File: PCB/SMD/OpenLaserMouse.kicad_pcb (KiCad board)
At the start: 2 copper layers, 56 x 84 mm, 24 parts, among them J1 Amiga_Conn, M1 ADNS-9800, Q1 IRLML6302TRPBF, SW2 LEFT, SW3 RIGHT

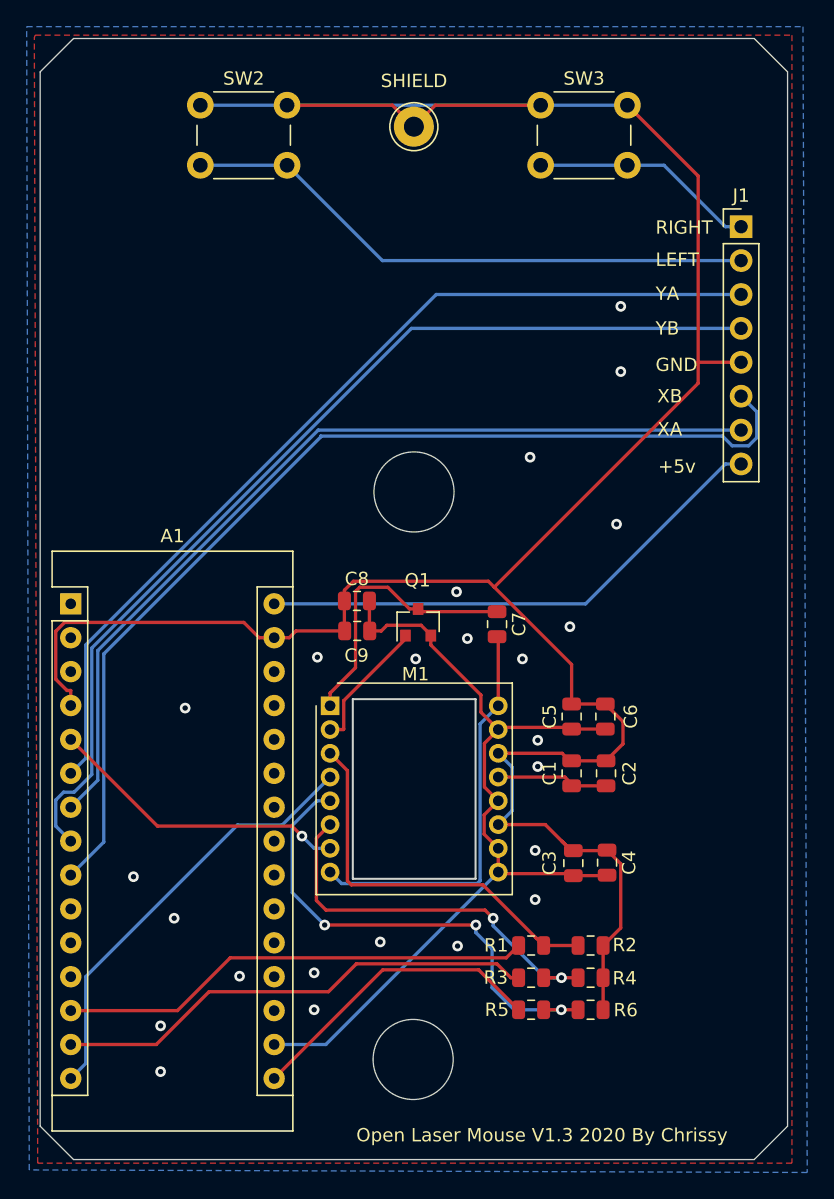
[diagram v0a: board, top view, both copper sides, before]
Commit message: Added ST Mouse PCB
Added ST Mouse PCB
Fixed Wrong Fillplane on Amiga PCB
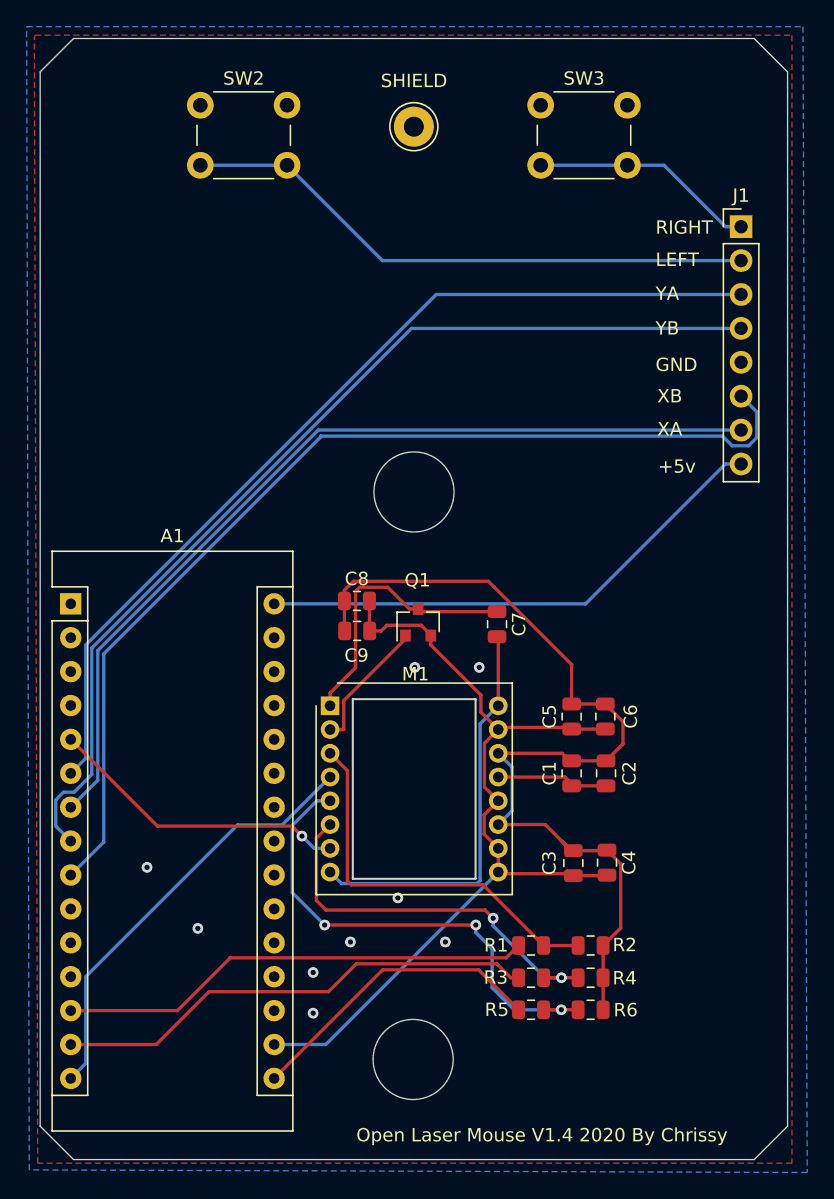
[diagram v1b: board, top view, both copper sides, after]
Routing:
- net GND: track 201.2 -> 72.1 mm, vias 0 -> 9
- net Net-(A1-Pad1): vias 24 -> 0
- added copper zone on B.Cu, net GND
- added copper zone on F.Cu, net GND
- removed copper zone on B.Cu, net Net-(A1-Pad1)
- removed copper zone on F.Cu, net Net-(A1-Pad1)
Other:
- board text added: "Open Laser Mouse V1.4 2020 By Chrissy"
- board text removed: "Open Laser Mouse V1.3 2020 By Chrissy"
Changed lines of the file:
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@@
     (thickness 1.6)
     (drawings 18)
-    (tracks 242)
+    (tracks 204)
     (zones 0)
     (modules 24)
@@
     (effects (font (size 1 1) (thickness 0.15)) (justify left))
   )
-  (gr_text "Open Laser Mouse V1.3 2020 By Chrissy" (at 77.597 122.174) (layer F.SilkS)
+  (gr_text "Open Laser Mouse V1.4 2020 By Chrissy" (at 77.597 122.174) (layer F.SilkS)
     (effects (font (size 1 1) (thickness 0.15)))
   )
@@
   (segment (start 79.1055 100.1612) (end 79.9465 101.002) (width 0.25) (layer F.Cu) (net 14) (status 20))
   (segment (start 81.9145 101.002) (end 81.915 101.002) (width 0.25) (layer F.Cu) (net 14) (status 30))
-  (segment (start 42.291 89.9795) (end 42.291 88.8542) (width 0.25) (layer F.Cu) (net 14) (status 10))
-  (segment (start 57.531 84.8995) (end 56.4057 84.8995) (width 0.25) (layer F.Cu) (net 14) (status 10))
-  (segment (start 56.4057 84.8995) (end 55.2596 83.7534) (width 0.25) (layer F.Cu) (net 14))
-  (segment (start 55.2596 83.7534) (end 41.8286 83.7534) (width 0.25) (layer F.Cu) (net 14))
-  (segment (start 41.8286 83.7534) (end 41.1657 84.4163) (width 0.25) (layer F.Cu) (net 14))
-  (segment (start 41.1657 84.4163) (end 41.1657 88.0103) (width 0.25) (layer F.Cu) (net 14))
-  (segment (start 41.1657 88.0103) (end 42.0096 88.8542) (width 0.25) (layer F.Cu) (net 14))
-  (segment (start 42.0096 88.8542) (end 42.291 88.8542) (width 0.25) (layer F.Cu) (net 14))
-  (segment (start 57.531 84.8995) (end 58.6563 84.8995) (width 0.25) (layer F.Cu) (net 14) (status 10))
-  (segment (start 58.6563 84.8995) (end 59.1643 84.3915) (width 0.25) (layer F.Cu) (net 14))
-  (segment (start 59.1643 84.3915) (end 62.9665 84.3915) (width 0.25) (layer F.Cu) (net 14) (status 20))
-  (segment (start 89.3011 64.262) (end 89.3011 65.8347) (width 0.25) (layer F.Cu) (net 14))
-  (segment (start 92.5195 64.262) (end 89.3011 64.262) (width 0.25) (layer F.Cu) (net 14) (status 10))
   (segment (start 62.9665 82.263) (end 62.9665 82.677) (width 0.25) (layer F.Cu) (net 14) (status 30))
   (segment (start 74.322 98.9) (end 75.3618 97.8602) (width 0.25) (layer B.Cu) (net 14) (status 10))
   (segment (start 75.3618 97.8602) (end 75.3618 94.5998) (width 0.25) (layer B.Cu) (net 14))
   (segment (start 75.3618 94.5998) (end 74.322 93.56) (width 0.25) (layer B.Cu) (net 14) (status 20))
-  (segment (start 58.5 45) (end 52 45) (width 0.25) (layer B.Cu) (net 14) (status 30))
-  (segment (start 84 45) (end 77.5 45) (width 0.25) (layer B.Cu) (net 14) (status 30))
-  (segment (start 77.5 45) (end 58.5 45) (width 0.25) (layer B.Cu) (net 14) (status 30))
   (segment (start 74.322 93.56) (end 79.1075 93.56) (width 0.25) (layer F.Cu) (net 14) (status 10))
   (segment (start 79.1075 93.56) (end 79.8195 94.272) (width 0.25) (layer F.Cu) (net 14) (status 20))
-  (segment (start 89.3011 64.262) (end 89.3011 50.3011) (width 0.25) (layer F.Cu) (net 14))
-  (segment (start 89.3011 50.3011) (end 84 45) (width 0.25) (layer F.Cu) (net 14) (status 20))
-  (segment (start 66.391 45) (end 58.5 45) (width 0.25) (layer F.Cu) (net 14) (status 20))
-  (segment (start 68 46.609) (end 66.391 45) (width 0.25) (layer F.Cu) (net 14) (status 10))
-  (segment (start 69.609 45) (end 77.5 45) (width 0.25) (layer F.Cu) (net 14) (status 20))
-  (segment (start 68 46.609) (end 69.609 45) (width 0.25) (layer F.Cu) (net 14) (status 10))
   (segment (start 62.7934 84.3684) (end 62.8165 84.3915) (width 0.25) (layer F.Cu) (net 14) (status 30))
   (segment (start 62.7934 82.1436) (end 62.7934 84.3684) (width 0.25) (layer F.Cu) (net 14) (status 30))
@@
   (segment (start 79.8195 90.0175) (end 79.8195 86.9061) (width 0.25) (layer F.Cu) (net 14) (status 10))
   (segment (start 79.8195 86.9061) (end 74.0246 81.1112) (width 0.25) (layer F.Cu) (net 14))
-  (segment (start 89.3011 65.8347) (end 74.0246 81.1112) (width 0.25) (layer F.Cu) (net 14))
   (segment (start 82.4362 100.8525) (end 82.4738 100.8149) (width 0.25) (layer F.Cu) (net 14) (status 30))
   (segment (start 79.9465 100.8525) (end 82.4362 100.8525) (width 0.25) (layer F.Cu) (net 14) (status 30))
@@
   (segment (start 73.58198 80.66858) (end 74.0246 81.1112) (width 0.25) (layer F.Cu) (net 14))
   (segment (start 62.7934 82.1436) (end 62.7934 81.3436) (width 0.25) (layer F.Cu) (net 14))
+  (via (at 51.816 106.68) (size 0.8) (drill 0.4) (layers F.Cu B.Cu) (net 14))
+  (via (at 48.006 102.108) (size 0.8) (drill 0.4) (layers F.Cu B.Cu) (net 14))
+  (via (at 70.358 107.696) (size 0.8) (drill 0.4) (layers F.Cu B.Cu) (net 14))
+  (via (at 63.246 107.696) (size 0.8) (drill 0.4) (layers F.Cu B.Cu) (net 14))
+  (via (at 60.452 109.982) (size 0.8) (drill 0.4) (layers F.Cu B.Cu) (net 14))
+  (via (at 60.452 113.03) (size 0.8) (drill 0.4) (layers F.Cu B.Cu) (net 14))
+  (via (at 66.802 104.394) (size 0.8) (drill 0.4) (layers F.Cu B.Cu) (net 14))
+  (via (at 68.072 87.122) (size 0.8) (drill 0.4) (layers F.Cu B.Cu) (net 14))
+  (via (at 72.898 87.122) (size 0.8) (drill 0.4) (layers F.Cu B.Cu) (net 14))
   (segment (start 75.8467 112.776) (end 72.855221 109.784521) (width 0.25) (layer F.Cu) (net 15))
   (segment (start 65.665979 109.784521) (end 57.531 117.9195) (width 0.25) (layer F.Cu) (net 15))
@@
   (segment (start 82.4362 102.7275) (end 82.4738 102.6899) (width 0.25) (layer F.Cu) (net 18) (status 30))
   (segment (start 79.9465 102.7275) (end 82.4362 102.7275) (width 0.25) (layer F.Cu) (net 18) (status 30))
-  (via (at 50.8635 90.17) (size 0.8) (drill 0.4) (layers F.Cu B.Cu) (net 19))
-  (via (at 83.185 76.3905) (size 0.8) (drill 0.4) (layers F.Cu B.Cu) (net 19))
-  (via (at 76.708 71.374) (size 0.8) (drill 0.4) (layers F.Cu B.Cu) (net 19))
-  (via (at 83.5025 64.9605) (size 0.8) (drill 0.4) (layers F.Cu B.Cu) (net 19))
-  (via (at 83.5025 60.071) (size 0.8) (drill 0.4) (layers F.Cu B.Cu) (net 19))
-  (via (at 79.6925 84.074) (size 0.8) (drill 0.4) (layers F.Cu B.Cu) (net 19))
-  (via (at 72.009 84.963) (size 0.8) (drill 0.4) (layers F.Cu B.Cu) (net 19))
-  (via (at 68.1355 86.487) (size 0.8) (drill 0.4) (layers F.Cu B.Cu) (net 19))
-  (via (at 60.7695 86.36) (size 0.8) (drill 0.4) (layers F.Cu B.Cu) (net 19))
-  (via (at 76.1365 86.487) (size 0.8) (drill 0.4) (layers F.Cu B.Cu) (net 19))
-  (via (at 77.2795 92.583) (size 0.8) (drill 0.4) (layers F.Cu B.Cu) (net 19))
-  (via (at 77.2795 94.5515) (size 0.8) (drill 0.4) (layers F.Cu B.Cu) (net 19))
-  (via (at 77.089 100.838) (size 0.8) (drill 0.4) (layers F.Cu B.Cu) (net 19))
-  (via (at 77.089 104.521) (size 0.8) (drill 0.4) (layers F.Cu B.Cu) (net 19))
-  (via (at 46.99 102.8065) (size 0.8) (drill 0.4) (layers F.Cu B.Cu) (net 19))
-  (via (at 50.038 105.918) (size 0.8) (drill 0.4) (layers F.Cu B.Cu) (net 19))
-  (via (at 49.022 117.4115) (size 0.8) (drill 0.4) (layers F.Cu B.Cu) (net 19))
-  (via (at 49.022 113.9825) (size 0.8) (drill 0.4) (layers F.Cu B.Cu) (net 19))
-  (via (at 54.9402 110.2614) (size 0.8) (drill 0.4) (layers F.Cu B.Cu) (net 19))
-  (via (at 71.2724 108.0008) (size 0.8) (drill 0.4) (layers F.Cu B.Cu) (net 19))
-  (via (at 65.4812 107.696) (size 0.8) (drill 0.4) (layers F.Cu B.Cu) (net 19))
-  (via (at 60.5282 112.776) (size 0.8) (drill 0.4) (layers F.Cu B.Cu) (net 19))
-  (via (at 60.5282 110.0074) (size 0.8) (drill 0.4) (layers F.Cu B.Cu) (net 19))
-  (via (at 71.1962 81.4578) (size 0.8) (drill 0.4) (layers F.Cu B.Cu) (net 19))
   (segment (start 74.322 95.34) (end 79.3125 95.34) (width 0.25) (layer F.Cu) (net 20) (status 10))
   (segment (start 79.3125 95.34) (end 79.8195 95.847) (width 0.25) (layer F.Cu) (net 20) (status 20))
@@
   (segment (start 67.668 82.7415) (end 66.04509 81.11859) (width 0.25) (layer F.Cu) (net 22))
   (segment (start 68.318 82.7415) (end 67.668 82.7415) (width 0.25) (layer F.Cu) (net 22))
-  (zone (net 19) (net_name "Net-(A1-Pad1)") (layer F.Cu) (hatch edge 0.508)
+  (zone (net 14) (net_name GND) (layer F.Cu) (hatch edge 0.508)
     (connect_pads (clearance 0.508))
     (min_thickness 0.254)
@@
     )
   )
-  (zone (net 19) (net_name "Net-(A1-Pad1)") (layer B.Cu) (hatch edge 0.508)
+  (zone (net 14) (net_name GND) (layer B.Cu) (hatch edge 0.508)
     (connect_pads (clearance 0.508))
     (min_thickness 0.254)
